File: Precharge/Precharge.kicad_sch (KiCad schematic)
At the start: 53 parts, among them J1 Conn_01x02, J2 Conn_01x02, J3 Molex MicroFit, J4 Conn_02x03_Counter_Clockwise, K1 KT12-1A-40L-THT, Q1 AO3400A, Q2 AO3400A, Q3 AO3400A, U1 LM393, U2 4N35, U3 4N35

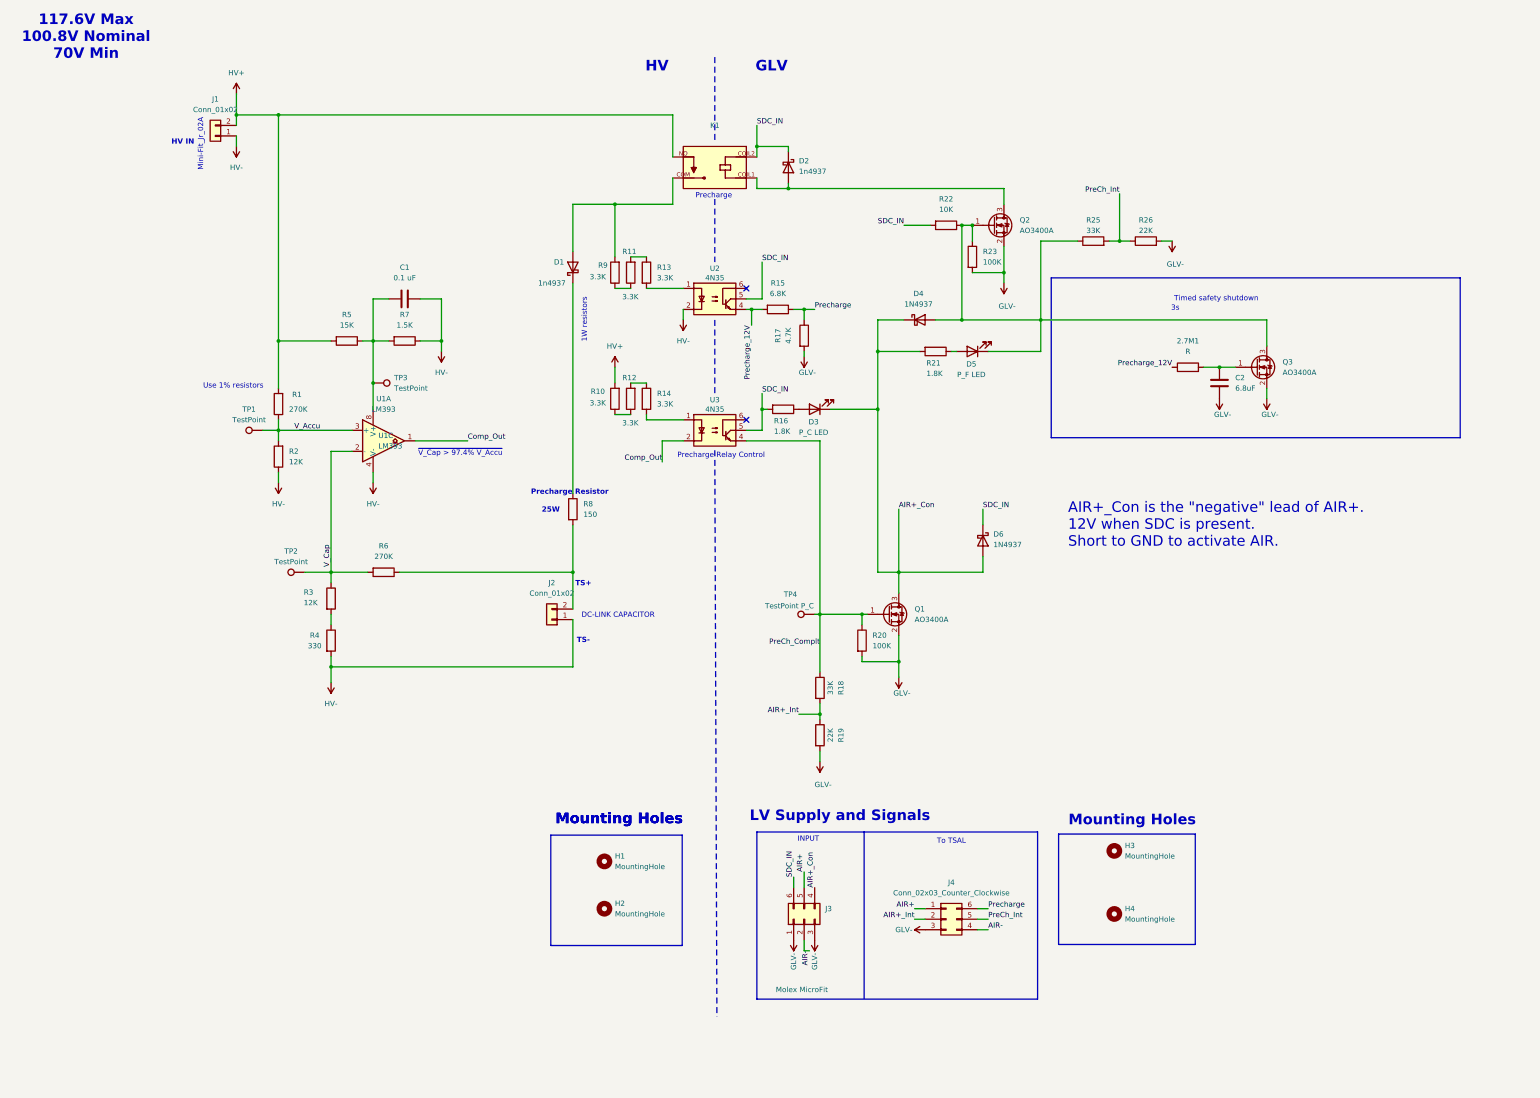
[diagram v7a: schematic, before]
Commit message: ADD TSAL boards and MOD Precharge
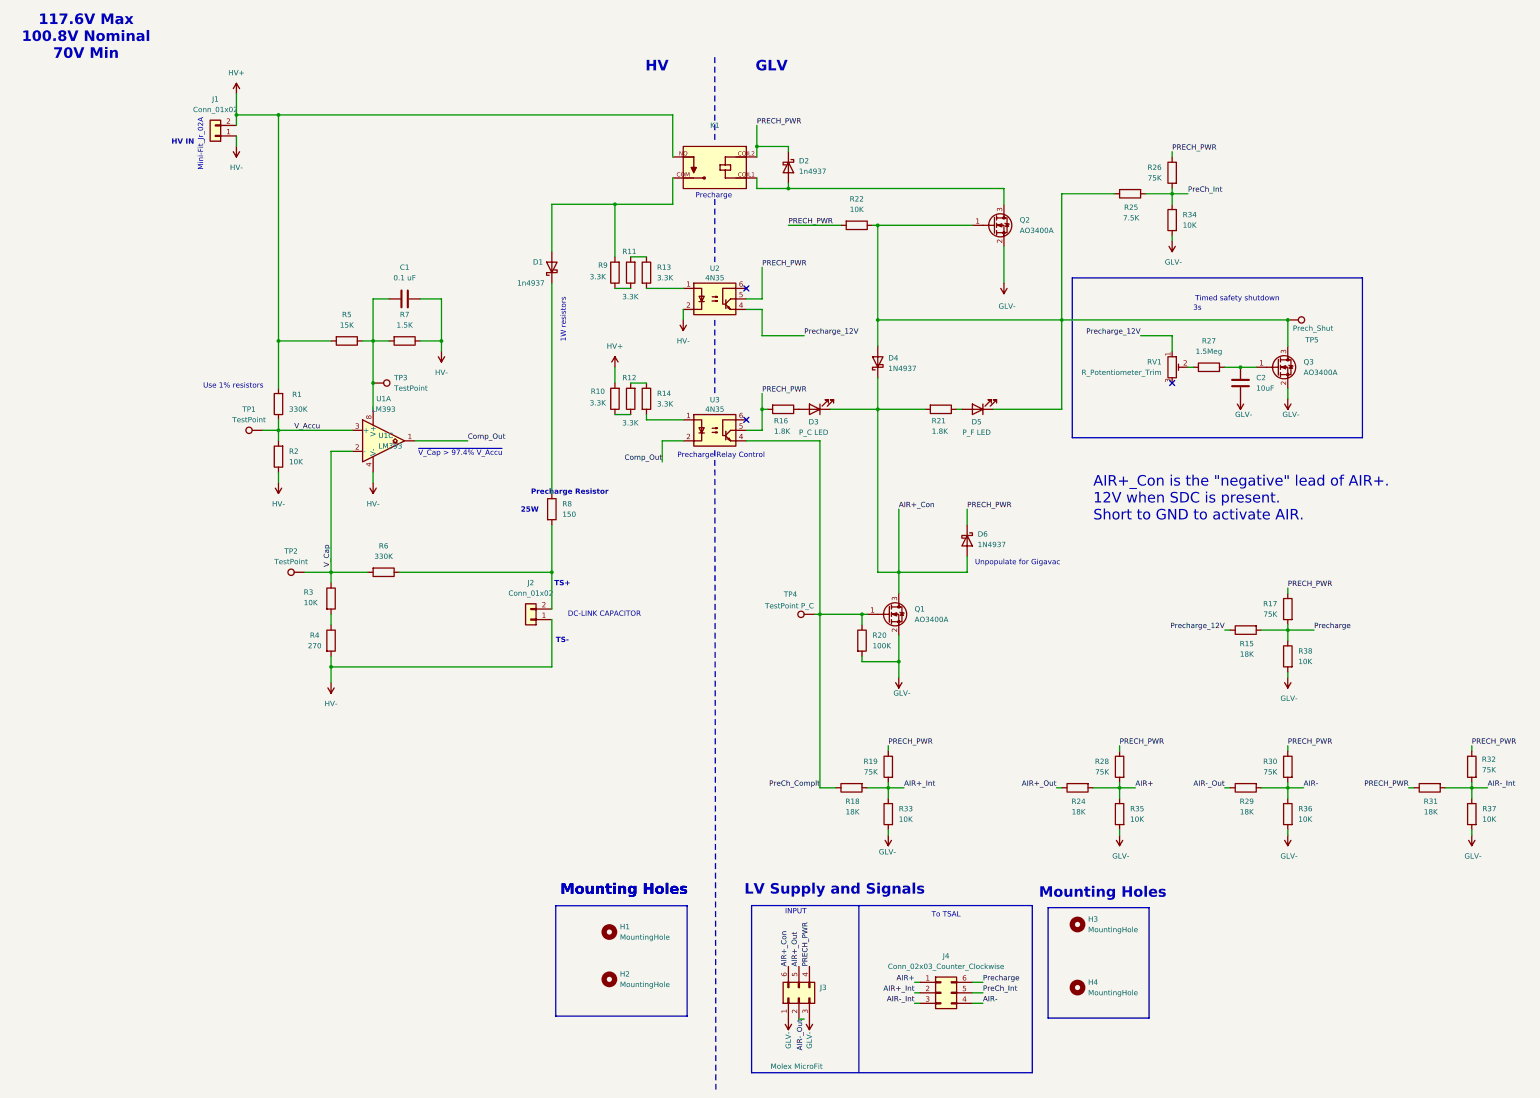
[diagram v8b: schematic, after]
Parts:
- removed R23: 100K, Resistor_SMD:R_0603_1608Metric_Pad0.98x0.95mm_HandSolder, symbol Device:R
- added R24, R29, R31: 18K, Resistor_SMD:R_0603_1608Metric_Pad0.98x0.95mm_HandSolder, symbol Device:R
- added R28, R30, R32: 75K, Resistor_SMD:R_0603_1608Metric_Pad0.98x0.95mm_HandSolder, symbol Device:R
- added R33, R34, R35, R36, R37, R38: 10K, Resistor_SMD:R_0603_1608Metric_Pad0.98x0.95mm_HandSolder, symbol Device:R
- added RV1: R_Potentiometer_Trim, Potentiometer_THT:Potentiometer_Bourns_3296W_Vertical, symbol Device:R_Potentiometer_Trim
- added TP5: Prech_Shut, Connector_Pin:Pin_D1.0mm_L10.0mm, symbol Connector:TestPoint
- C2: value 6.8uF -> 10uF
- R1, R6: value 270K -> 330K; Comments (none) -> 1% tolerance
- R15: value 6.8K -> 18K
- R17: value 4.7K -> 75K
- R18: value 33K -> 18K
- R19, R26: value 22K -> 75K
- R2, R3: value 12K -> 10K; Comments (none) -> 1% tolerance
- R25: value 33K -> 7.5K
- R27: renamed from 2.7M1; value R -> 1.5Meg
- R4: value 330 -> 270; Comments (none) -> 1% tolerance
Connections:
- net AIR+: now also R24.2, R28.2, R35.1; no longer J3.5 (Pin_5)
- net AIR+_Con: now also J3.6 (Pin_6); no longer J3.4 (Pin_4)
- net AIR+_Int: now also R19.2, R33.1; no longer R19.1
- net AIR-: now also R29.2, R30.2, R36.1; no longer J3.2 (Pin_2)
- net GLV-: now also R33.2, R34.2, R35.2, R36.2, R37.2, R38.2; no longer J4.3 (Pin_3), R17.2, R19.2, R26.2
- net PreCh_Int: now also R26.2, R34.1; no longer R26.1
- net Precharge: now also R15.2, R17.2, R38.1; no longer R15.1, R17.1
- net Precharge_12V: now also R15.1, RV1.1; no longer R15.2, R27.1
- net at D4.2 (A), D5.1 (K), Q2.1 (G)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: now also TP5.1
- net SDC_IN renamed PRECH_PWR
- net PRECH_PWR: now also J3.4 (Pin_4), R17.1, R19.1, R26.1, R28.1, R30.1, R31.1, R32.1; no longer J3.6 (Pin_6)
- new net: R27.1, RV1.2
- new net AIR+_Out: J3.5 (Pin_5), R24.1
- new net AIR-_Int: J4.3 (Pin_3), R31.2, R32.2, R37.1
- new net AIR-_Out: J3.2 (Pin_2), R29.1
- no-connect marks 2 -> 3
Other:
- note added: "Unpopulate for Gigavac"
- moved on the sheet: C2, D1, D5, D6, H1, H2, H3, H4, J2, J3, J4, Q3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
